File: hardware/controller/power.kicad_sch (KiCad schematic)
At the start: 26 parts, among them J4 XT-60, Q1 SUD50P04-08, SW5 SW_SPST, U6 LM1117MP-3.3, U7 LV14340

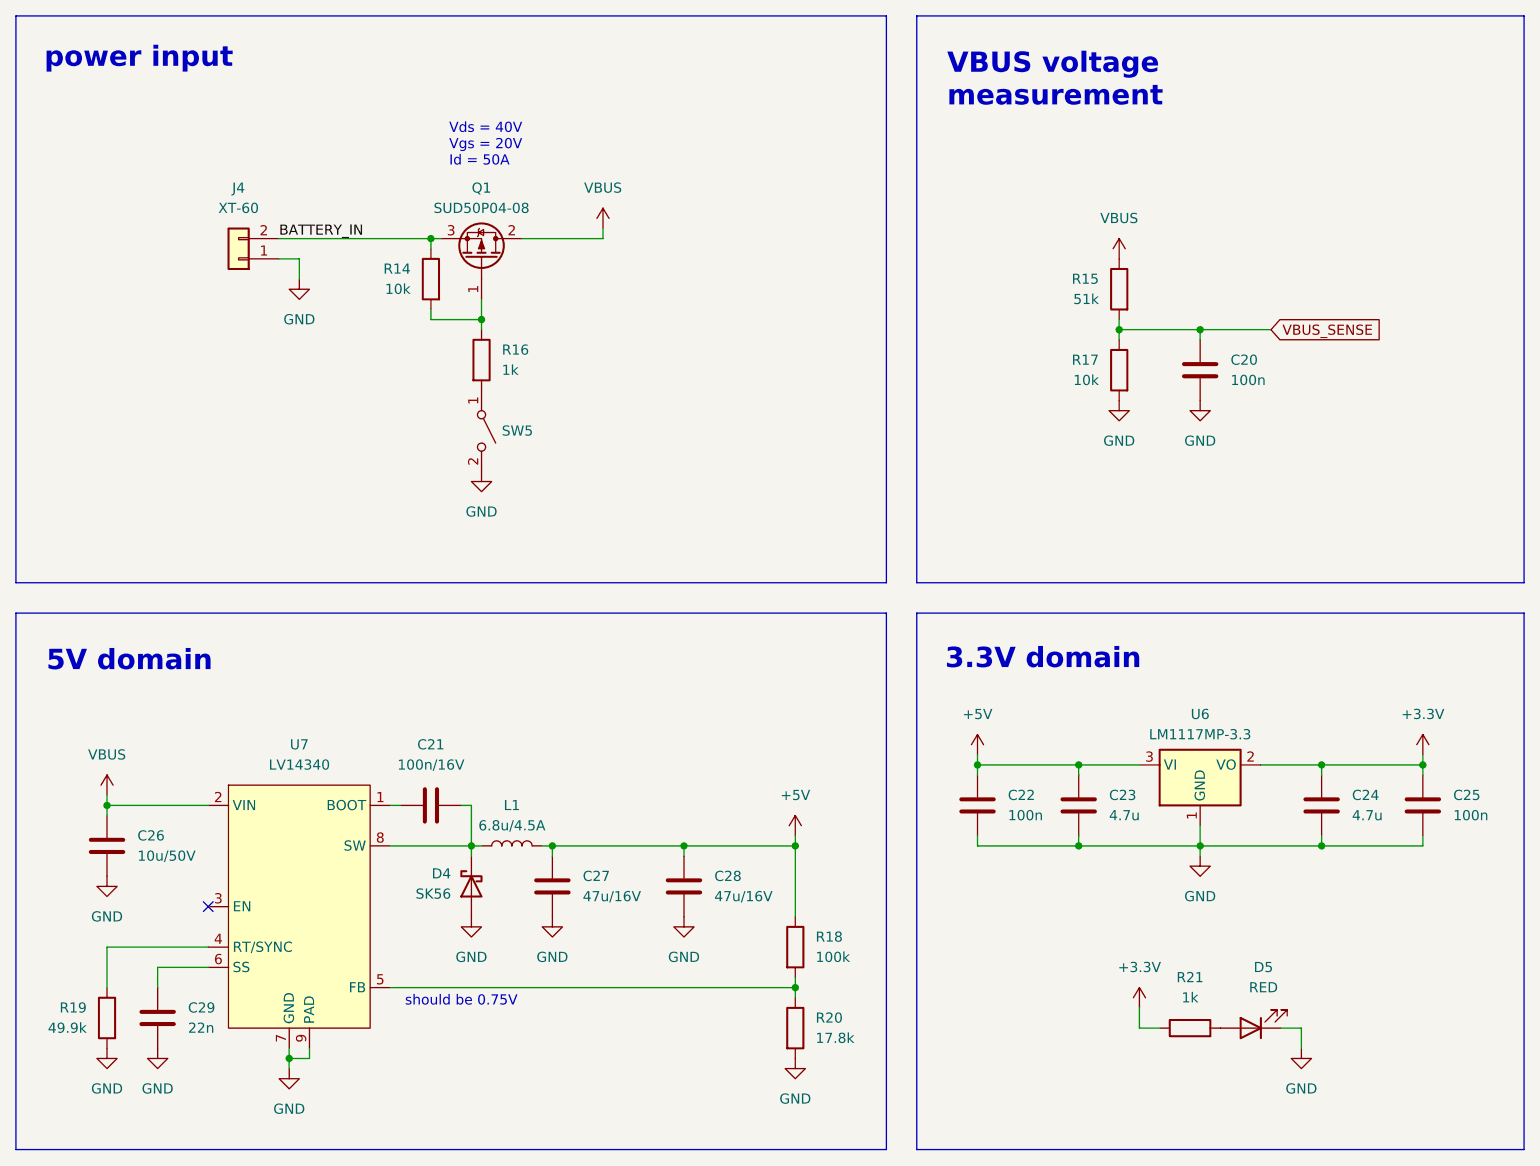
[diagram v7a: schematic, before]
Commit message: back to LM2105, remove USB-C from STM
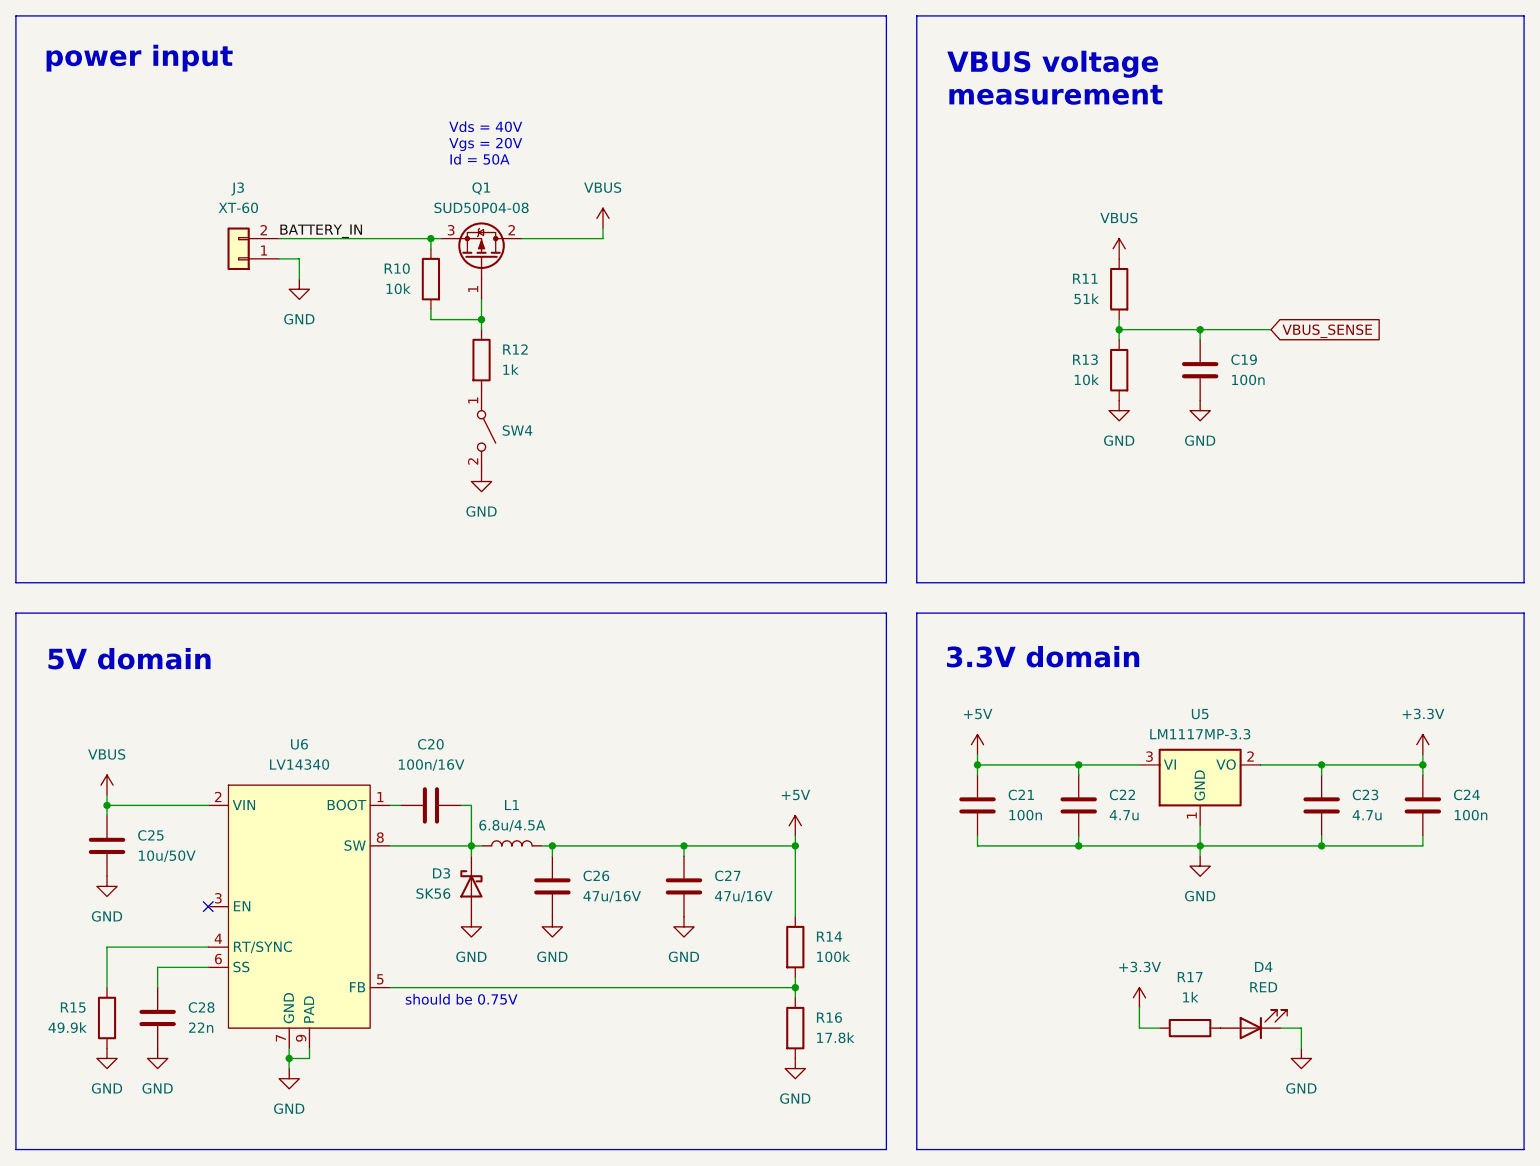
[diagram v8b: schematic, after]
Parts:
- renumbered C20 to C19, C21 to C20, C22 to C21, C23 to C22, C24 to C23, C25 to C24, C26 to C25, C27 to C26, C28 to C27, C29 to C28, D4 to D3, D5 to D4, J4 to J3, R14 to R10, R15 to R11, R16 to R12, R17 to R13, R18 to R14, R19 to R15, R20 to R16, R21 to R17, SW5 to SW4, U6 to U5, U7 to U6
